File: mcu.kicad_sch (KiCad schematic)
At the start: 26 parts, among them J2 USB-C, J3 UART0, J4 I2C / Qwiic, J5 Spare IO, J6 Rail break-out, SW1 RESET, SW2 BOOT, U4 ESP32-S3-WROOM-1-N16R8, U5 USBLC6-2SC6

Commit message: Generate the 4-layer board: placed, DRC-clean, ready to route
gen/generate_pcb.py (runs under KiCad 9's bundled Python) builds
esp32s3-can-sd-logger.kicad_pcb from the same part/net tables as the
schematic generator: real library footprints, every pad netted, and
zone-based placement -- harness connectors on the left edge, analog
channel columns and the ESP32 with its antenna overhanging the top edge
(module keepout falls off-board), USB-C/microSD/buttons on the right,
battery front end and both bucks in the bottom band, GND and +3V3
inner-plane zones, JLC-compatible 0.2mm minimum drill.

84 x 72 mm. kicad-cli pcb drc: zero violations; the 335 unconnected
items are the unrouted ratsnest.

Also adds the project footprint library (TDK ACT45B CAN choke built from
the datasheet land pattern) and a placement render under plots/.

Co-Authored-By: Claude Fable 5 <noreply@anthropic.com>
Claude-Session: https://claude.ai/code/session_01DhNbL25h25p8VFCjRfJik9
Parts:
- J2: MPN (none) -> HRO TYPE-C-31-M-12
- SW1: MPN (none) -> TL3342F160QG; Note (none) -> Genuine E-Switch is scarce at LCSC; any 5.2mm gull-wing tac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
- SW2: MPN (none) -> TL3342F160QG
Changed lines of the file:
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@@
+      (effects (font (size 1.27 1.27)) hide)
+    )
+    (property "MPN" "TL3342F160QG" (at 62.23 123.92 0)
+      (effects (font (size 1.27 1.27)) hide)
+    )
+    (property "Note" "Genuine E-Switch is scarce at LCSC; any 5.2mm gull-wing tact fits" (at 62.23 123.92 0)
       (effects (font (size 1.27 1.27)) hide)
     )
@@
     )
     (property "Datasheet" "~" (at 62.23 154.4 0)
+      (effects (font (size 1.27 1.27)) hide)
+    )
+    (property "MPN" "TL3342F160QG" (at 62.23 154.4 0)
       (effects (font (size 1.27 1.27)) hide)
     )
@@
       (effects (font (size 1.27 1.27)) hide)
     )
+    (property "MPN" "HRO TYPE-C-31-M-12" (at 62.23 258.54 0)
+      (effects (font (size 1.27 1.27)) hide)
+    )

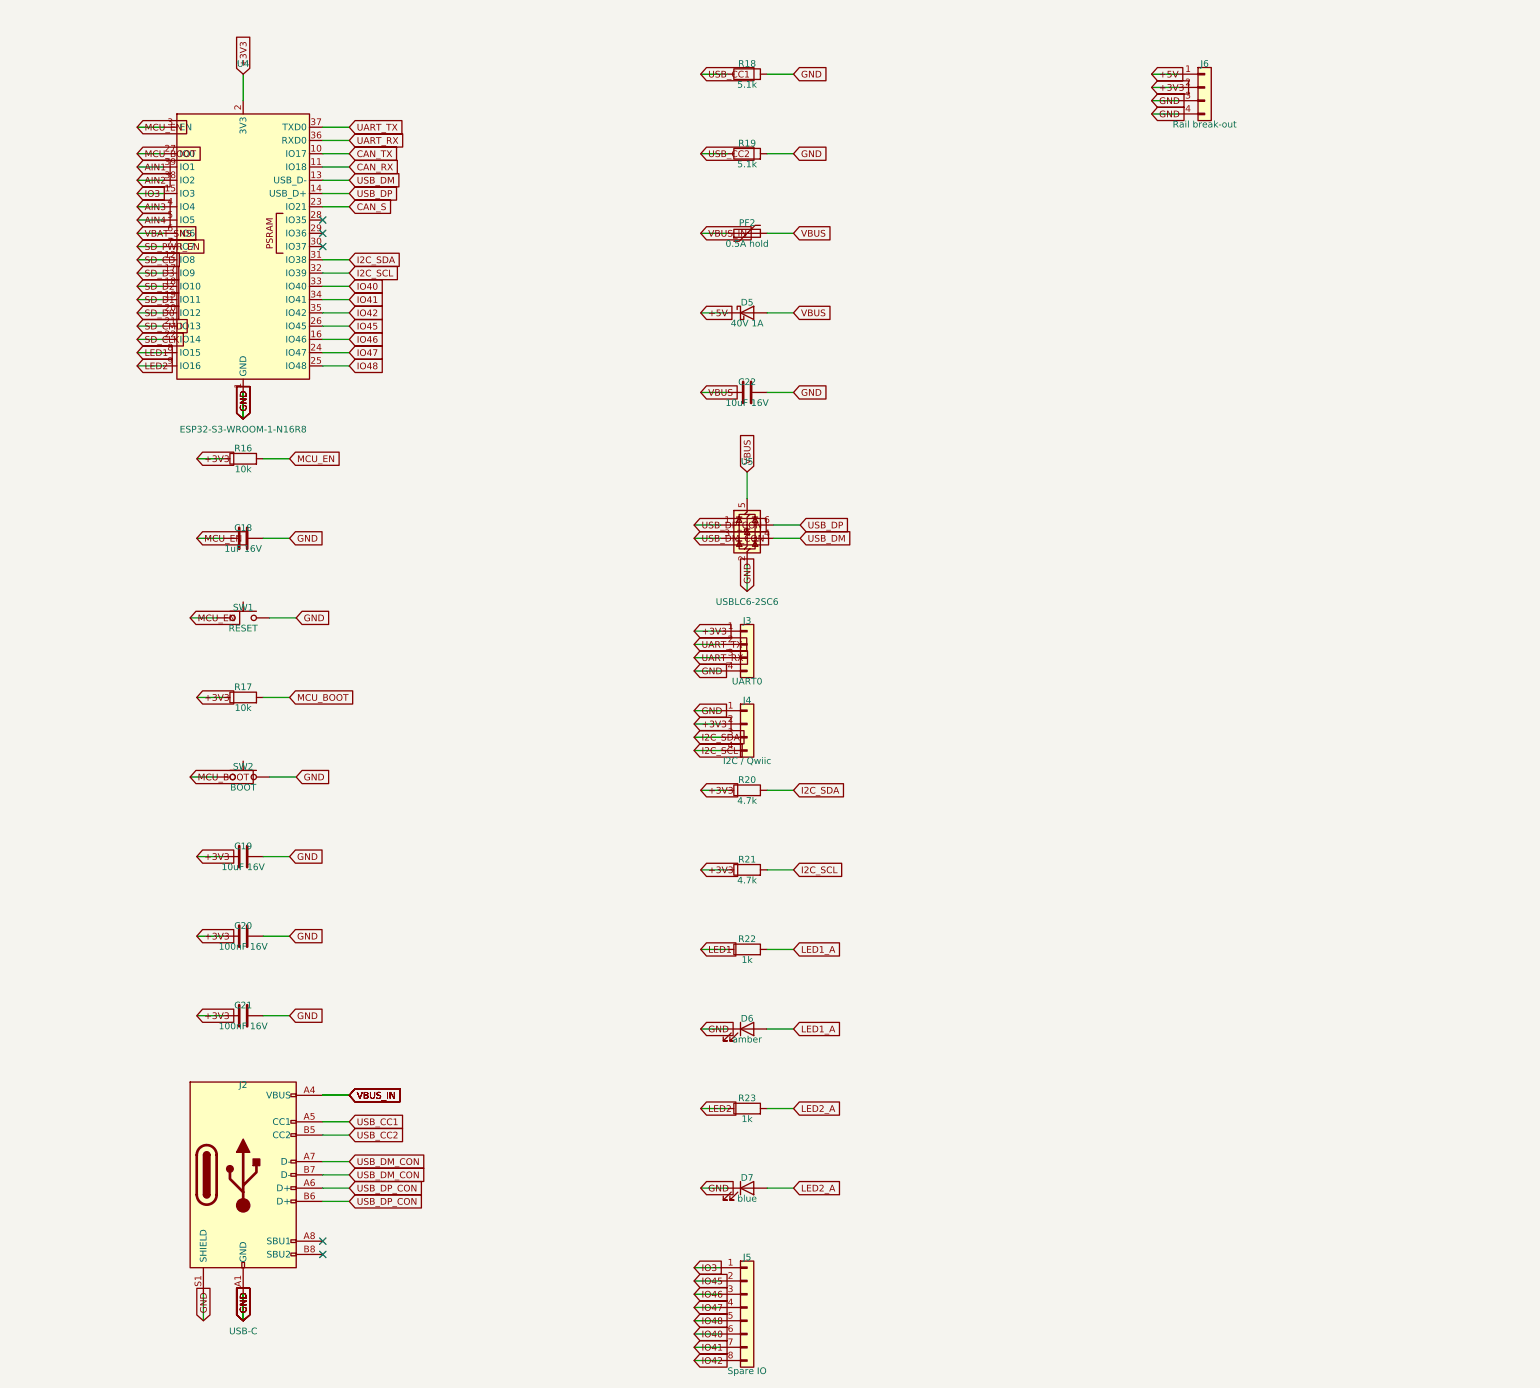
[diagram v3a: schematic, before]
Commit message: Add WS2812 5V DIN, SPI breakout, and PCB handoff docs.
Shift-light header uses a 74AHCT1G125 so GPIO48 drives real 5V data; SPI lands on IO40/41/42/47 with spare IO3/45/46 kept. README §10 covers remaining routing for the next agent.

Co-authored-by: Cursor <cursoragent@cursor.com>
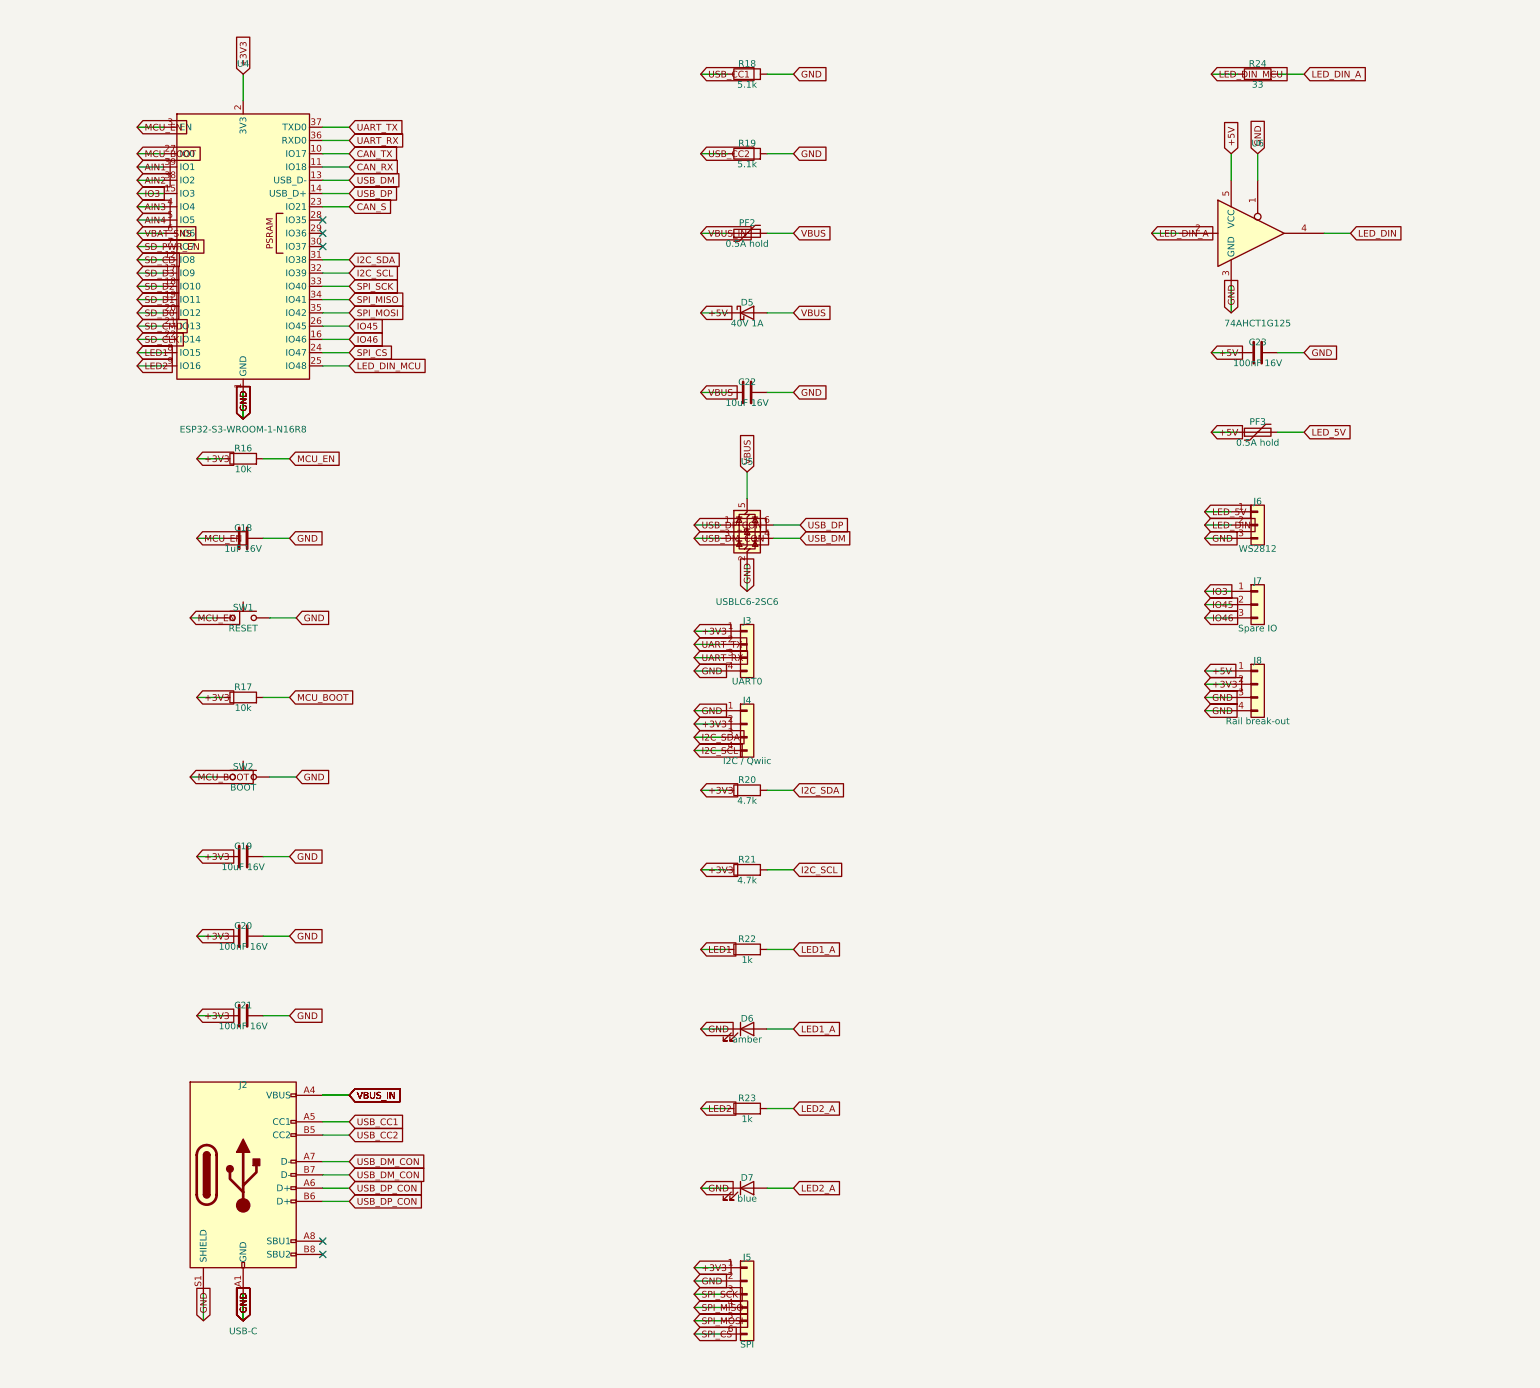
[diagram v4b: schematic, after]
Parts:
- added C23: 100nF 16V, Capacitor_SMD:C_0805_2012Metric, symbol Device:C
- added J7: Spare IO, Connector_PinHeader_2.54mm:PinHeader_1x03_P2.54mm_Vertical, symbol Connector_Generic:Conn_01x03
- added J8: Rail break-out, Connector_PinHeader_2.54mm:PinHeader_1x04_P2.54mm_Vertical, symbol Connector_Generic:Conn_01x04
- added PF3: 0.5A hold, Resistor_SMD:R_1206_3216Metric, symbol Device:Polyfuse
- added R24: 33, Resistor_SMD:R_0805_2012Metric, symbol Device:R
- added U6: 74AHCT1G125, Package_TO_SOT_SMD:SOT-23-5, symbol 74xGxx:74AHCT1G125
- J5: value Spare IO -> SPI; footprint Connector_PinHeader_2.54mm:PinHeader_1x08_P2.54mm_Vertical -> Connector_PinHeader_2.54mm:PinHeader_1x06_P2.54mm_Vertical; symbol Connector_Generic:Conn_01x08 -> Connector_Generic:Conn_01x06; Note IO3/IO45/IO46 are strapping pins -- leave floating at boot -> IO40 SCK / IO41 MISO / IO42 MOSI / IO47 CS -- GPIO-matrix S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
- J6: value Rail break-out -> WS2812; footprint Connector_PinHeader_2.54mm:PinHeader_1x04_P2.54mm_Vertical -> Connector_PinHeader_2.54mm:PinHeader_1x03_P2.54mm_Vertical; symbol Connector_Generic:Conn_01x04 -> Connector_Generic:Conn_01x03; Note (none) -> Shift-light header: +5V / 5V-logic DIN / GND
- U4: Note 16MB flash / 8MB octal PSRAM. Pins 28-30 (IO35/36/37) are consumed by the octal PSRAM and must stay unconnected. -> 16MB flash / 8MB octal PSRAM. Pins 28-30 (IO35/36/37) are consumed by the octal PSRAM and must stay unconnected. IO3/IO45/IO46 on the spare header are strapping pins -- leave floating at boot.
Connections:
- net +3V3: now also J5.1 (Pin_1), J8.2 (Pin_2); no longer J6.2 (Pin_2)
- net +5V: now also C23.1, J8.1 (Pin_1), PF3.1, U6.5 (VCC); no longer J6.1 (Pin_1)
- net GND: now also J5.2 (Pin_2), C23.2, J8.3 (Pin_3), J8.4 (Pin_4), U6.1, U6.3 (GND); no longer J6.4 (Pin_4)
- net IO3: now also J7.1 (Pin_1); no longer J5.1 (Pin_1)
- net IO45: now also J7.2 (Pin_2); no longer J5.2 (Pin_2)
- net IO46: now also J7.3 (Pin_3); no longer J5.3 (Pin_3)
- net IO40 renamed SPI_CS
- net SPI_CS: now also U4.24 (IO47); no longer U4.33 (IO40)
- net IO41 renamed SPI_MISO
- net SPI_MISO: now also J5.4 (Pin_4); no longer J5.7 (Pin_7)
- net IO42 renamed SPI_MOSI
- net SPI_MOSI: now also J5.5 (Pin_5); no longer J5.8 (Pin_8)
- removed net IO47: J5.4 (Pin_4), U4.24 (IO47)
- net IO48 renamed LED_DIN_MCU
- net LED_DIN_MCU: now also R24.1; no longer J5.5 (Pin_5)
- new net LED_5V: J6.1 (Pin_1), PF3.2
- new net LED_DIN: J6.2 (Pin_2), U6.4
- new net LED_DIN_A: R24.2, U6.2
- new net SPI_SCK: J5.3 (Pin_3), U4.33 (IO40)

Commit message: Schematic: power symbols and readable text placement (items 1-2 of 5)
The schematic was a netlist drawn as a picture: 486 global labels for 108
nets, roughly four per net, every part an island with a name flag on each
pin and no wires between anything. You could not trace a circuit by eye.
That is a fair description of a document that fails at the one thing a
schematic is for, and it is on me -- the generator was built to produce a
correct netlist and the drawing was an afterthought.

Two of the five agreed fixes are in:

Rails are power symbols. GND, +3V3, +5V, +5VS, +VBAT, VBUS and SD_VDD now
carry a proper power symbol instead of a net-name label -- 190 of them,
taking the label count from 486 to 296. Where KiCad has no stock symbol
for a rail a generic one is instantiated with its Value overridden, which
is how KiCad names a power net; validate.py re-extracts through KiCad and
compares node-for-node, so a wrong guess there would fail the build rather
than quietly merge two rails. PWR_FLAG keeps a label: pairing it with a
power symbol makes an island of two symbols that declares a rail and
connects to nothing visible.

Text no longer collides. Labels were all justified left, so any label
pointing back at its own component ran its text over the body -- RON_5V
across R4, SW_5V across L1; they now justify away from the part.
Reference and value sat hard against the symbol, so a pin leaving the top
or bottom put its stub and power symbol straight through them: "LM5164
(5V)" printed through the GND symbol under U2. Both now clear the stub,
and the row height accounts for it so the clearance does not just push
the collision into the next row. Power symbol references are hidden, as
they are in every schematic.

Also fixed: the packer wrapped on height but never on width, so the power
sheet silently ran off the 420 mm page -- two symbols landed at x = 422.9
where ERC reported them unconnected and nothing else complained. It now
fails loudly.

Items 3-5 (real hierarchy, w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
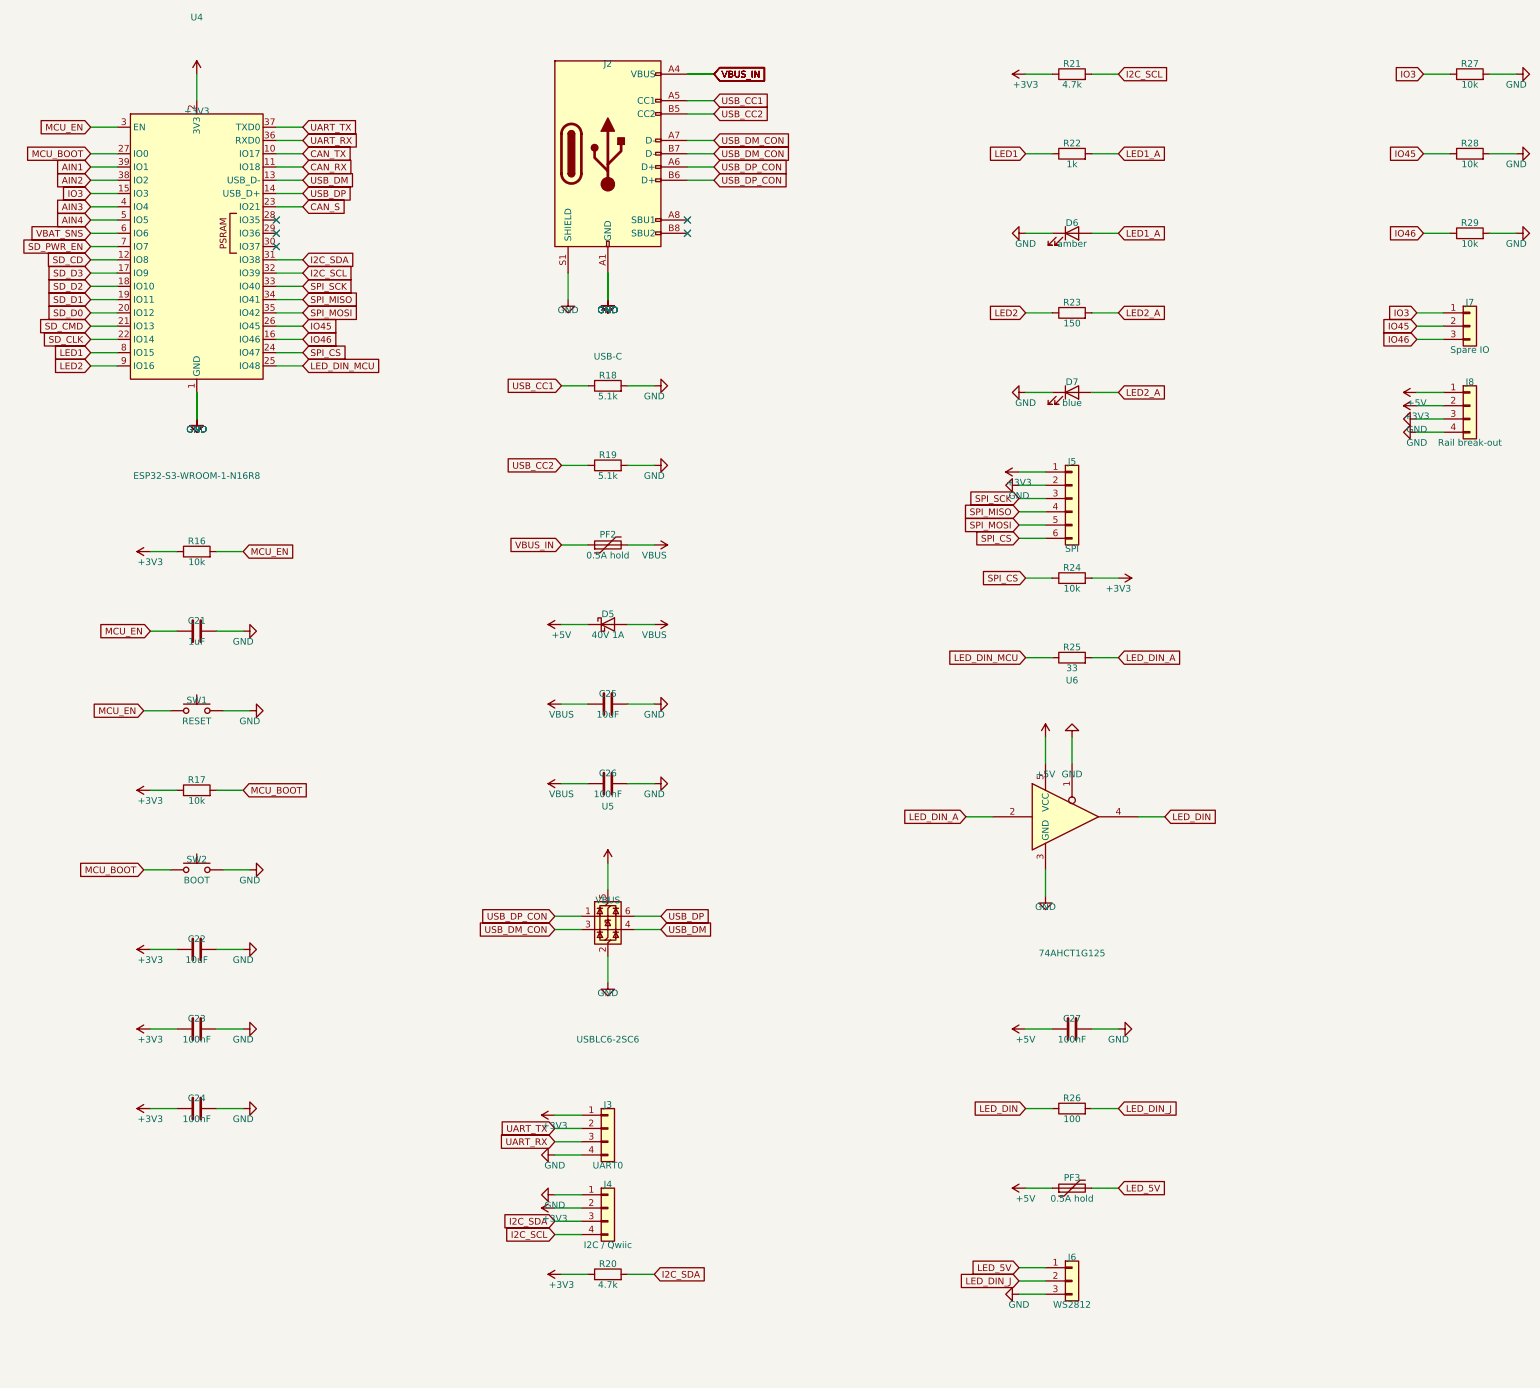
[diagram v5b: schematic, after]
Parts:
- removed C18: 1uF 16V, Capacitor_SMD:C_0805_2012Metric, symbol Device:C
- removed C19: 10uF 16V, Capacitor_SMD:C_1206_3216Metric, symbol Device:C
- removed C20: 100nF 16V, Capacitor_SMD:C_0805_2012Metric, symbol Device:C
- added C24, C26, C27: 100nF, Capacitor_SMD:C_0805_2012Metric, symbol Device:C
- added C25: 10uF, Capacitor_SMD:C_1206_3216Metric, symbol Device:C
- added R25: 33, Resistor_SMD:R_0805_2012Metric, symbol Device:R
- added R26: 100, Resistor_SMD:R_0805_2012Metric, symbol Device:R
- added R27, R28, R29: 10k, Resistor_SMD:R_0805_2012Metric, symbol Device:R
- C21: value 100nF 16V -> 1uF; Note (none) -> EN reset delay; Voltage (none) -> 16V
- C22: value 10uF 16V -> 10uF; Voltage (none) -> 16V
- C23: value 100nF 16V -> 100nF; Note AHCT decoupling -> (none); Voltage (none) -> 16V
- J7: Note IO3/IO45/IO46 are strapping pins -- leave floating at boot -> IO3/IO45/IO46 are strapping pins, each with a 10k pull-down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
- R23: value 1k -> 150; Note (none) -> Blue Vf sits close to 3.288V, so 1k here gave about 0.19mA 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
- R24: value 33 -> 10k; Note Edge-rate limit into the level shifter -> Holds an attached slave deselected until firmware drives IO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
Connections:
- net +3V3: now also C22.1, C23.1, R24.2, C24.1; no longer C21.1
- net +5V: now also C27.1; no longer C23.1
- net GND: now also C24.2, C25.2, C26.2, C27.2, R27.2, R28.2, R29.2
- net IO3: now also R27.1
- net IO45: now also R28.1
- net IO46: now also R29.1
- net LED_DIN: now also R26.1; no longer J6.2 (Pin_2)
- net LED_DIN_A: now also R25.2; no longer R24.2
- net LED_DIN_MCU: now also R25.1; no longer R24.1
- net MCU_EN: now also C21.1
- net SPI_CS: now also R24.1
- net VBUS: now also C25.1, C26.1; no longer C22.1
- new net LED_DIN_J: J6.2 (Pin_2), R26.2
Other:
- moved on the sheet: C21, C22, C23, D5, D6, D7, J2, J3, J4, J5, J6, J7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
